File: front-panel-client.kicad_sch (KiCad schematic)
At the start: 9 parts, among them IC16 PMV20ENR, IC18 PMV20ENR, J4 855-M50-3500542

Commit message: first round of revisions
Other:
- moved on the sheet: IC18

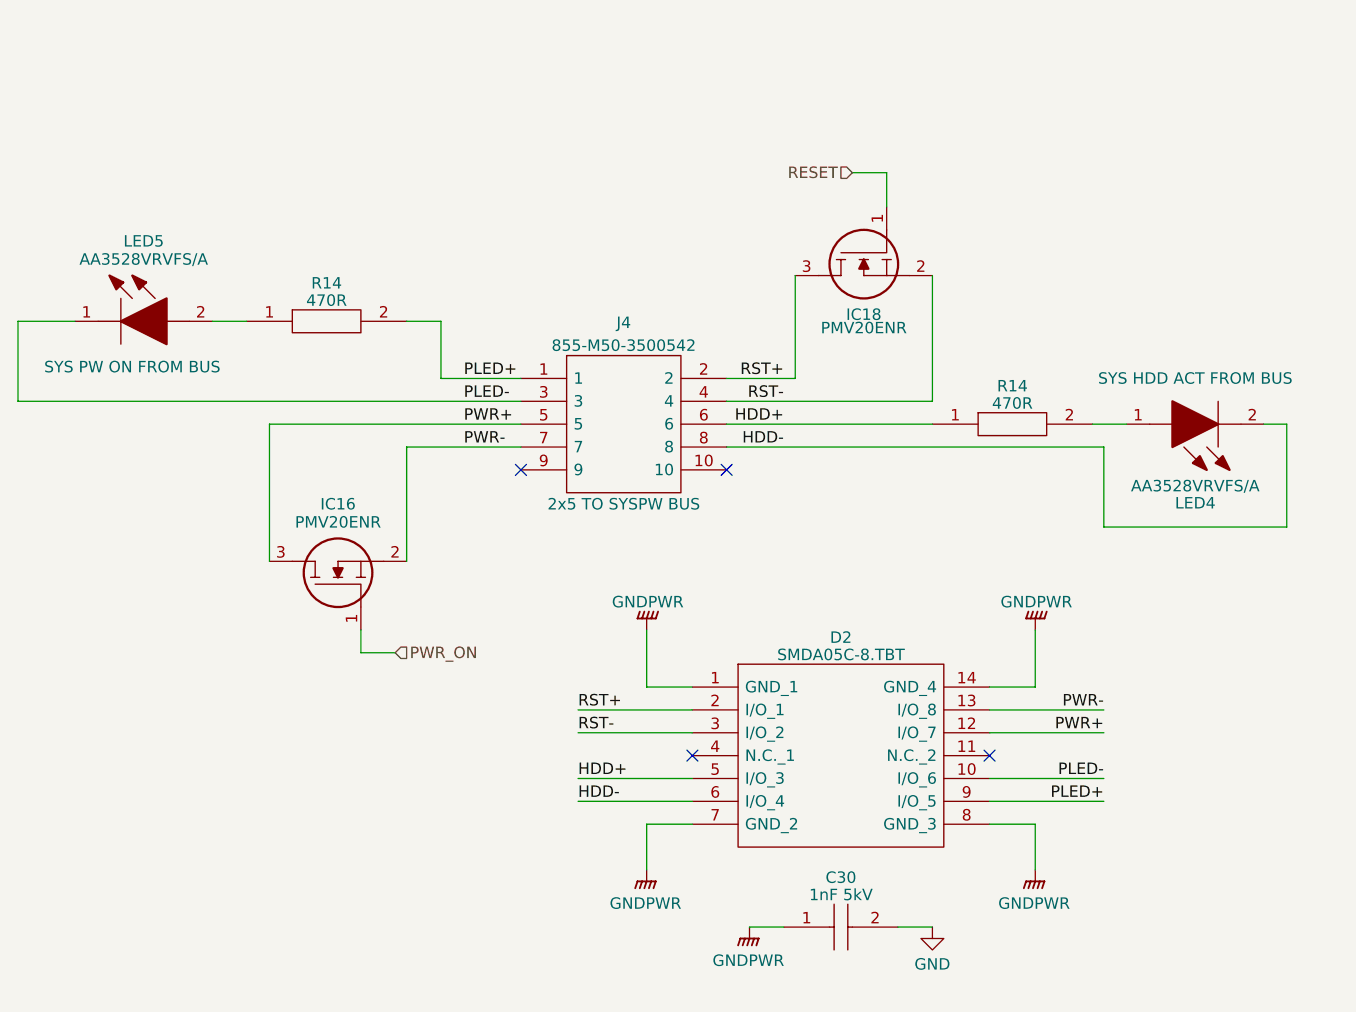
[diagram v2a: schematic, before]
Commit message: fully move to new MCU configuration
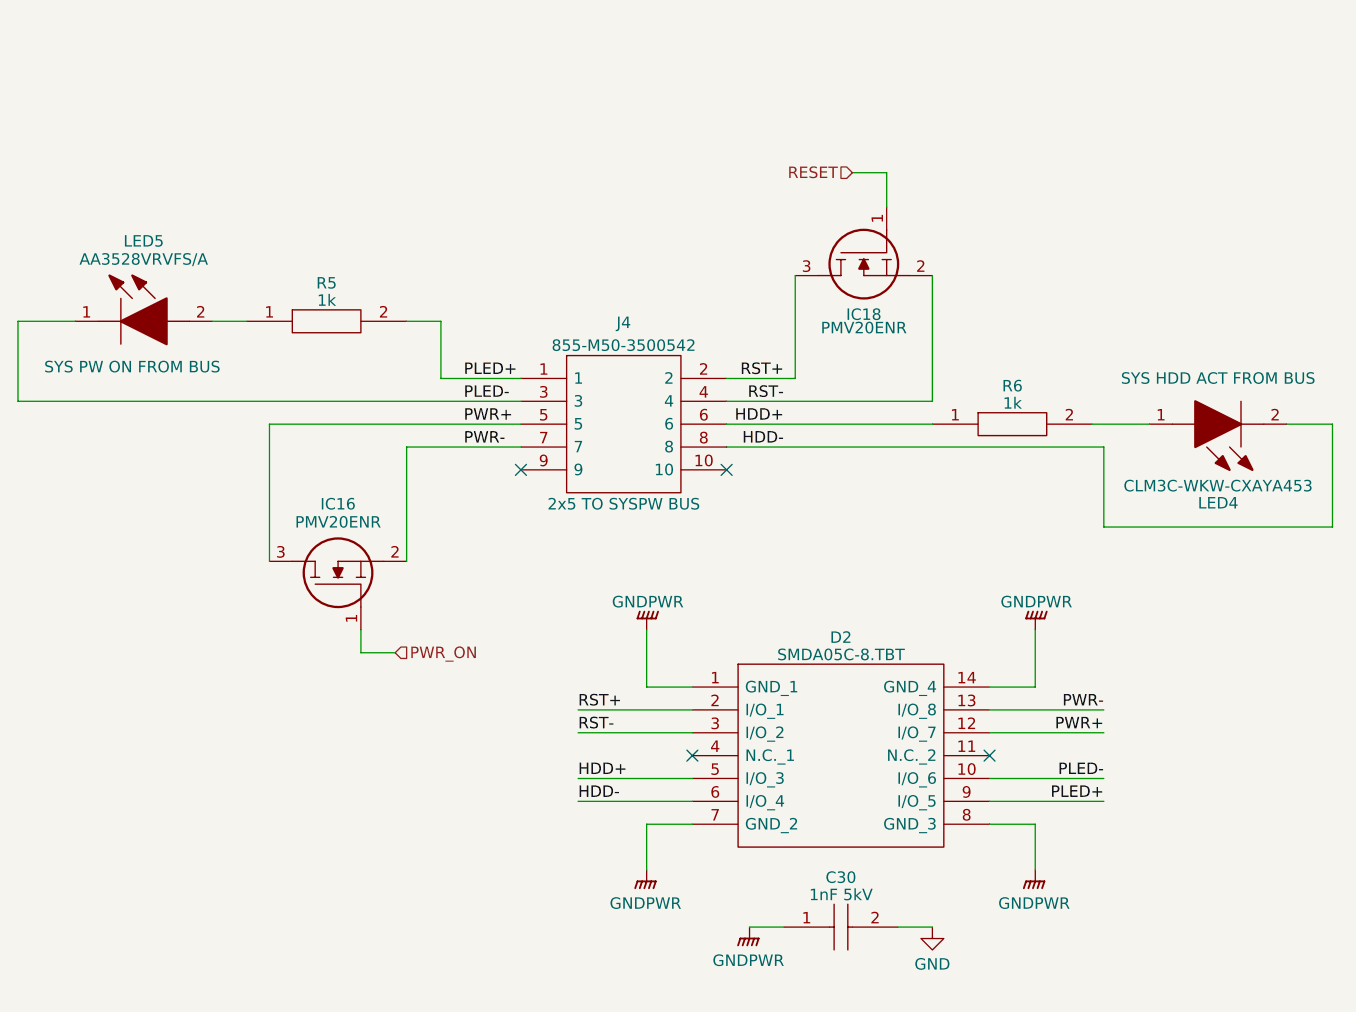
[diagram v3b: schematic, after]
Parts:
- removed R14 (x2): 470R, RESC2012X60N, symbol SamacSys_Parts:AC0805FR-07470RL
- added R5, R6: 1k, RESC2012X60N, symbol SamacSys_Parts:SG73P2ATTD102J
- LED4: value AA3528VRVFS/A -> CLM3C-WKW-CXAYA453
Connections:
- net HDD+: now also R6.1
- net PLED+: now also R5.2
- net at LED5.2: now also R5.1
- net at LED4.1: now also R6.2
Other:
- moved on the sheet: LED4

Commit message: first few boards laid out
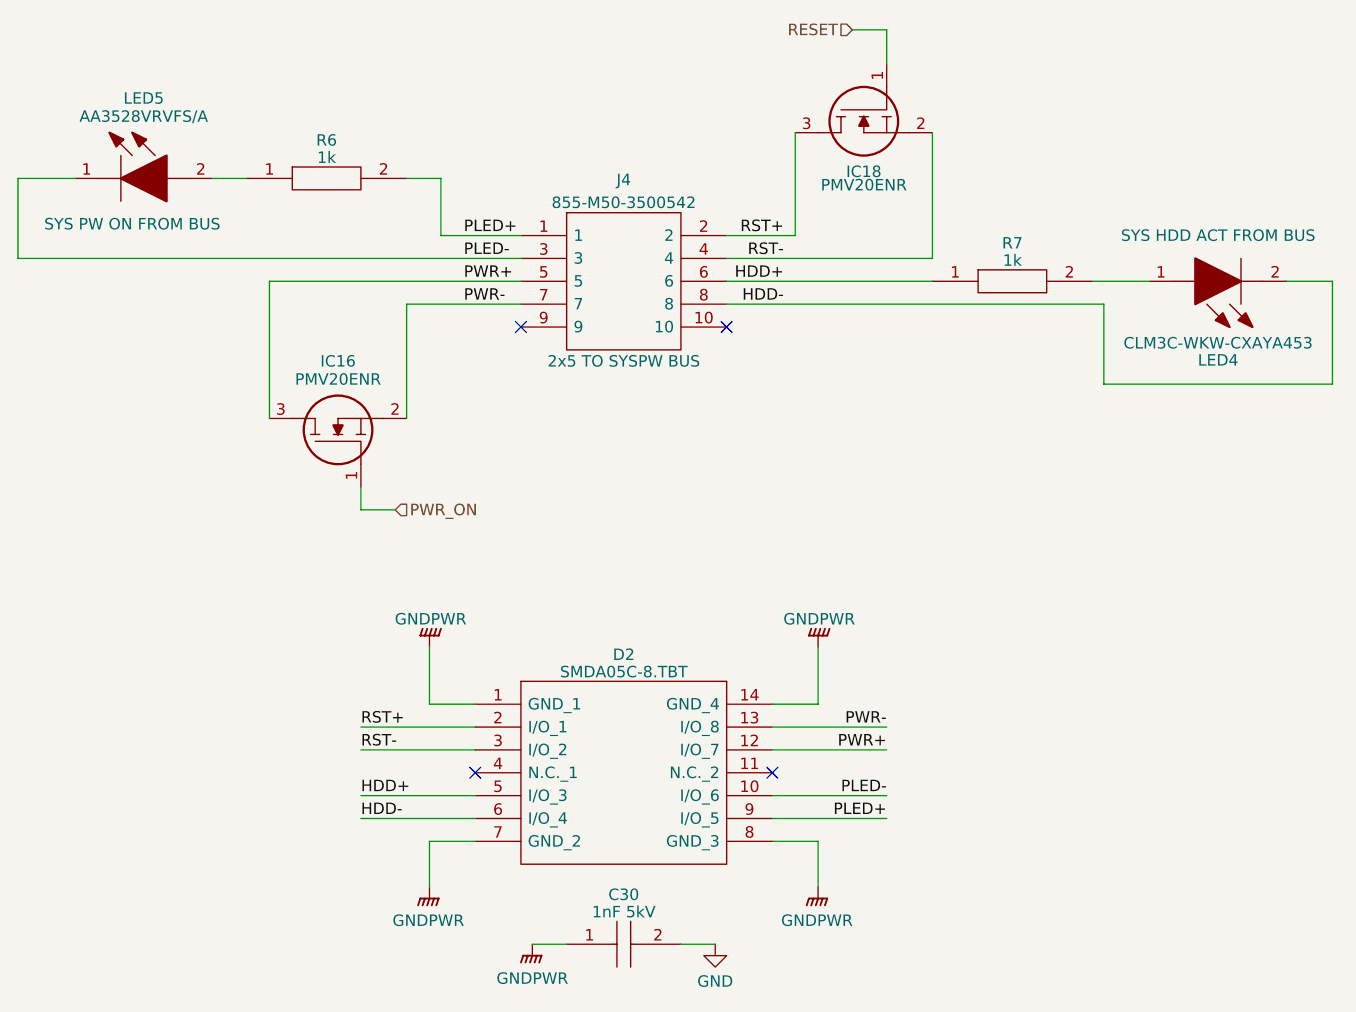
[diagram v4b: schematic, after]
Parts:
- renumbered R5 to R6, R6 to R7
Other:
- moved on the sheet: C30, D2, IC16, IC18, J4, LED4, LED5, R6, R7

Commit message: first panelization of entire modular dev board
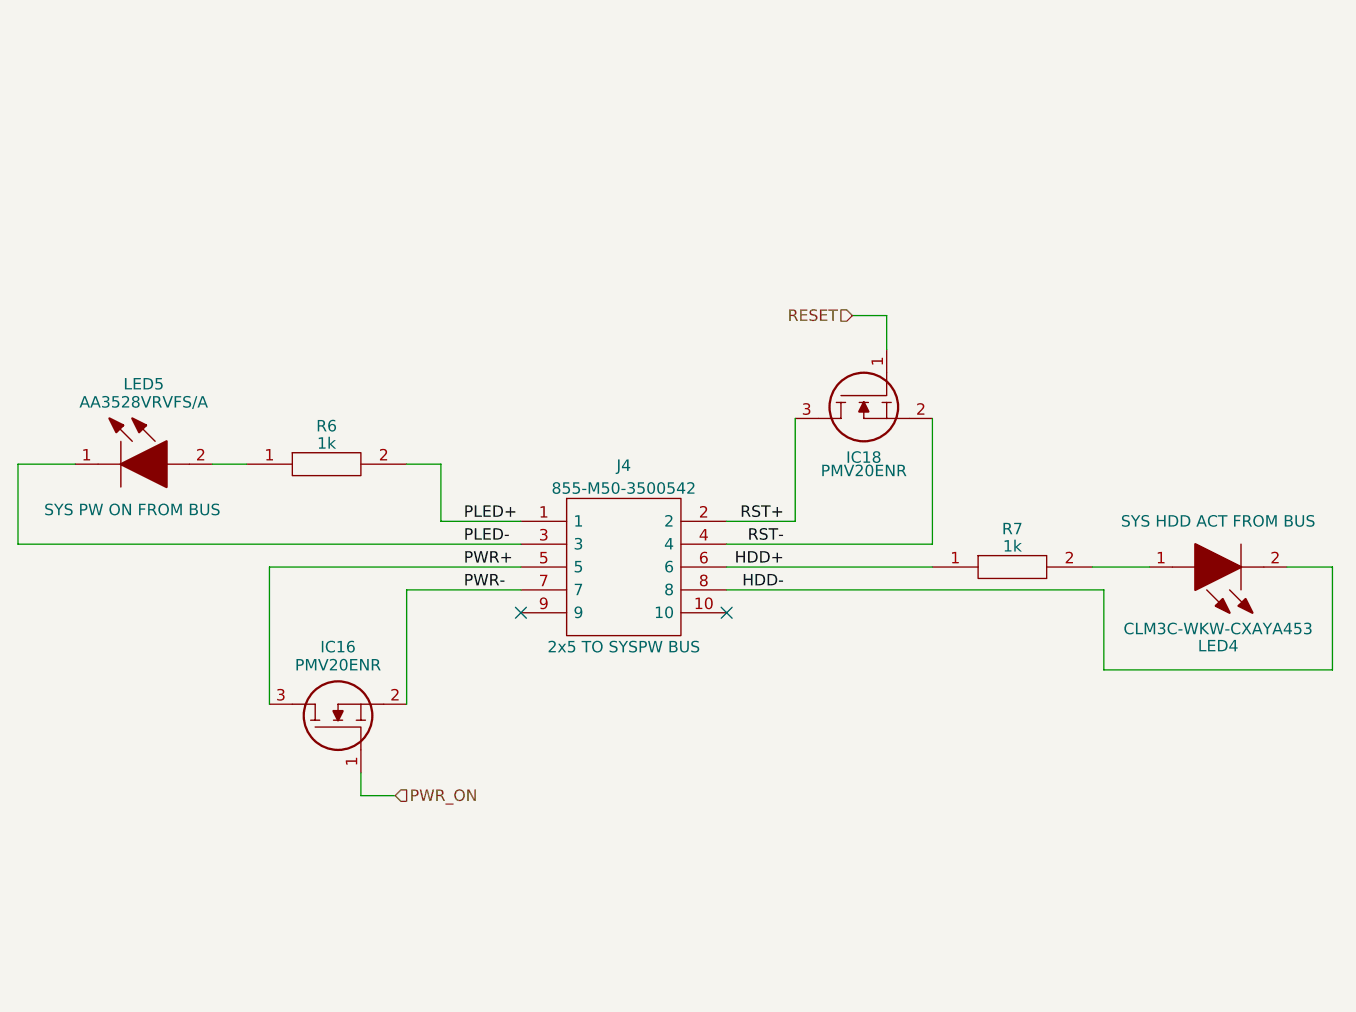
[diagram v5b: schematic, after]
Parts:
- removed C30: 1nF 5kV, CAPC5664X270N, symbol SamacSys_Parts:HV2225Y102KXMATHV
- removed D2: SMDA05C-8.TBT, SOIC127P600X175-14N, symbol SamacSys_Parts:SMDA05C-8.TBT
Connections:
- no-connect marks 4 -> 2
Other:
- moved on the sheet: IC16, IC18, J4, LED4, LED5, R6, R7

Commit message: initial board layout
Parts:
- J4: value 855-M50-3500542 -> 67996-110HLF; footprint SamacSys_Parts:M503500542 -> HDRV10W67P254_2X5_1270X483X858P; symbol SamacSys_Parts:M50-3500542 -> SamacSys_Parts:67996-110HLF; Arrow Part Number (none) -> 67996-110HLF; Arrow Price/Stock (none) -> https://www.arrow.com/en/products/67996-110hlf/amphenol-fci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; Height 4.15 -> 8.58; Manufacturer_Name Harwin -> Amphenol Communications Solutions; Manufacturer_Part_Number M50-3500542 -> 67996-110HLF; Mouser Part Number 855-M50-3500542 -> 649-67996-110HLF; Mouser Price/Stock https://www.mouser.co.uk/ProductDetail/Harwin/M50-3500542?q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 -> https://www.mouser.co.uk/ProductDetail/Amphenol-FCI/67996-1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
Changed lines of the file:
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@@
     )
   )
-  (symbol (lib_id "SamacSys_Parts:M50-3500542") (at 133.35 100.965 0) (unit 1)
+  (symbol (lib_id "SamacSys_Parts:67996-110HLF") (at 133.35 100.965 0) (unit 1)
     (in_bom yes) (on_board yes) (dnp no)
     (property "Reference" "J4" (at 144.78 94.776 0)
       (effects (font (size 1.27 1.27)))
     )
-    (property "Value" "855-M50-3500542" (at 144.78 97.3129 0)
+    (property "Value" "67996-110HLF" (at 144.78 97.3129 0)
       (effects (font (size 1.27 1.27)))
     )
-    (property "Footprint" "SamacSys_Parts:M503500542" (at 152.4 98.425 0)
+    (property "Footprint" "HDRV10W67P254_2X5_1270X483X858P" (at 152.4 98.425 0)
       (effects (font (size 1.27 1.27)) (justify left) hide)
     )
-    (property "Datasheet" "https://datasheet.datasheetarchive.com/originals/distributors/SFDatasheet-1/sf-00022684.pdf" (at 152.4 100.965 0)
+    (property "Datasheet" "https://cdn.amphenol-cs.com/media/wysiwyg/files/drawing/67996.pdf" (at 152.4 100.965 0)
       (effects (font (size 1.27 1.27)) (justify left) hide)
     )
-    (property "Description" "Header 2x5way DIL VERT Pin HARWIN M50-35 Series, 1.27mm Pitch 10 Way 2 Row Straight PCB Header, Solder Termination, 1A" (at 152.4 103.505 0)
+    (property "Description" "BergStik, Board to Board connector, Unshrouded vertical header, Through Hole, Double Row, 10 Positions, 2.54 mm (0.100in) Pitch" (at 152.4 103.505 0)
       (effects (font (size 1.27 1.27)) (justify left) hide)
     )
-    (property "Height" "4.15" (at 152.4 106.045 0)
+    (property "Height" "8.58" (at 152.4 106.045 0)
       (effects (font (size 1.27 1.27)) (justify left) hide)
     )
-    (property "Manufacturer_Name" "Harwin" (at 152.4 108.585 0)
+    (property "Manufacturer_Name" "Amphenol Communications Solutions" (at 152.4 108.585 0)
       (effects (font (size 1.27 1.27)) (justify left) hide)
     )
-    (property "Manufacturer_Part_Number" "M50-3500542" (at 152.4 111.125 0)
+    (property "Manufacturer_Part_Number" "67996-110HLF" (at 152.4 111.125 0)
       (effects (font (size 1.27 1.27)) (justify left) hide)
     )
-    (property "Mouser Part Number" "855-M50-3500542" (at 152.4 113.665 0)
+    (property "Mouser Part Number" "649-67996-110HLF" (at 152.4 113.665 0)
       (effects (font (size 1.27 1.27)) (justify left) hide)
     )
-    (property "Mouser Price/Stock" "https://www.mouser.co.uk/ProductDetail/Harwin/M50-3500542?qs=9fQaSFfsqsyXI0P9tFOVoQ%3D%3D" (at 152.4 116.205 0)
+    (property "Mouser Price/Stock" "https://www.mouser.co.uk/ProductDetail/Amphenol-FCI/67996-110HLF?qs=zh4O8xspOuxgf2RA9jR3ZQ%3D%3D" (at 152.4 116.205 0)
       (effects (font (size 1.27 1.27)) (justify left) hide)
     )
-    (property "Arrow Part Number" "" (at 152.4 118.745 0)
+    (property "Arrow Part Number" "67996-110HLF" (at 152.4 118.745 0)
       (effects (font (size 1.27 1.27)) (justify left) hide)
     )
-    (property "Arrow Price/Stock" "" (at 152.4 121.285 0)
+    (property "Arrow Price/Stock" "https://www.arrow.com/en/products/67996-110hlf/amphenol-fci?region=nac" (at 152.4 121.285 0)
       (effects (font (size 1.27 1.27)) (justify left) hide)
     )
@@
       (project "Oro Link rev2"
         (path "/e89dcd22-1250-4a5b-b778-1c95a0dd623d/6eeb4496-d532-42b5-95b8-3d397c9a21d1"
-          (reference "J20") (unit 1)
+          (reference "J2") (unit 1)
         )
       )
